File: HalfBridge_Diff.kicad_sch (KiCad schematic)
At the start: 3 parts, among them J5 Conn_01x04, U3 MAX3284E, U5 MAX3284E

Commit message: quad diff receiver
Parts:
- removed J5: Conn_01x04, Connector_Molex:Molex_PicoBlade_53261-0471_1x04-1MP_P1.25mm_Horizontal, symbol Connector_Generic:Conn_01x04
- added C2, C26, C3: 100n, Capacitor_SMD:C_0603_1608Metric_Pad1.08x0.95mm_HandSolder, symbol Device:C
- added J5: Conn_01x04_Shielded, My_Connector:Samtec_T1M-04-X-SH-L_1x04-1SH_P1.0mm_Terminal_Horizontal_Latch, symbol Connector_Generic_Shielded:Conn_01x04_Shielded
- added R18, R19: R, Resistor_SMD:R_0603_1608Metric_Pad0.98x0.95mm_HandSolder, symbol Device:R
- added U6: 74AUC2GU04, Package_TO_SOT_SMD:SOT-23-6_Handsoldering, symbol 74xGxx:74AUC2GU04
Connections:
- net gnd: now also C2.2, C26.1, C3.2, J5.SH (Shield), U6.2 (GND)
- net ina_d: now also U6.6; no longer U3.3 (RO)
- net ina_da: now also J5.4 (Pin_4), R18.1
- net ina_db: now also J5.3 (Pin_3), R18.2
- net inb_d: now also U6.4; no longer U5.3 (RO)
- net inb_da: now also J5.2 (Pin_2), R19.1
- net inb_db: now also J5.1 (Pin_1), R19.2
- net vcc: now also C2.1, C26.2, C3.1, U6.5 (VCC)
- new net ina_nd: U3.3 (RO), U6.1
- new net inb_nd: U5.3 (RO), U6.3
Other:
- moved on the sheet: U3

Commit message: not gate
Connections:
- net ina_d: now also U6.4; no longer U6.6
- net ina_nd: now also U6.3; no longer U6.1
- net inb_d: now also U6.6; no longer U6.4
- net inb_nd: now also U6.1; no longer U6.3
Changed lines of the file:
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@@
 		(lib_id "74xGxx:74AUC2GU04")
 		(at 161.29 109.22 0)
-		(unit 1)
+		(unit 2)
 		(exclude_from_sim no)
 		(in_bom yes)
@@
 				(path "/3c187ffa-7f66-4861-b077-b6965c821fc2/6db083ab-29ba-4c62-9810-6a6595b985fc"
 					(reference "U6")
-					(unit 1)
+					(unit 2)
 				)
 			)
@@
 		(lib_id "74xGxx:74AUC2GU04")
 		(at 161.29 142.24 0)
-		(unit 2)
+		(unit 1)
 		(exclude_from_sim no)
 		(in_bom yes)
@@
 				(path "/3c187ffa-7f66-4861-b077-b6965c821fc2/6db083ab-29ba-4c62-9810-6a6595b985fc"
 					(reference "U6")
-					(unit 2)
-				)
-			)
+					(unit 1)
+				)
+			)

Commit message: new optical diff xor
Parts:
- removed C26: 100n, Capacitor_SMD:C_0603_1608Metric_Pad1.08x0.95mm_HandSolder, symbol Device:C
- removed U6: 74AUC2GU04, Package_TO_SOT_SMD:SOT-23-6_Handsoldering, symbol 74xGxx:74AUC2GU04
- added J7: Conn_01x02, Connector_PinHeader_2.54mm:PinHeader_1x02_P2.54mm_Vertical, symbol Connector_Generic:Conn_01x02
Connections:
- net ina_nd is gone; now on net ina_d: U3.3 (RO)
- net inb_nd is gone; now on net inb_d: U5.3 (RO)
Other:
- moved on the sheet: C2, C3, R18, R19, U3, U5

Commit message: diff circuit
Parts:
- removed J5: Conn_01x04_Shielded, My_Connector:Samtec_T1M-04-X-SH-L_1x04-1SH_P1.0mm_Terminal_Horizontal_Latch, symbol Connector_Generic_Shielded:Conn_01x04_Shielded
- added C33: 100n, Capacitor_SMD:C_0603_1608Metric_Pad1.08x0.95mm_HandSolder, symbol Device:C
- added J10, J11, J12, J8, J9: Conn_01x02, Connector_PinHeader_2.54mm:PinHeader_1x02_P2.54mm_Vertical, symbol Connector_Generic:Conn_01x02
- added J14: Conn_01x02_Shielded, My_Connector:SAMTEC_T1M-02-F-SV-L-P, symbol Connector_Generic_Shielded:Conn_01x02_Shielded
- added R24: R, Resistor_SMD:R_0603_1608Metric_Pad0.98x0.95mm_HandSolder, symbol Device:R
- added R25, R26, R27: R, Resistor_SMD:R_0603_1608Metric, symbol Device:R
- added U9: MAX3284E, Package_TO_SOT_SMD:SOT-23-6_Handsoldering, symbol Interface_UART:MAX3284E
- J7: now not fitted
- renumbered C2 to C31, C3 to C32, R18 to R22, R19 to R23, U3 to U7, U5 to U8
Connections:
- net gnd: now also C33.2, J10.2 (Pin_2), J11.2 (Pin_2), J12.2 (Pin_2), J14.SH (Shield), U9.2 (GND)
- net ina_d: now also J10.1 (Pin_1), R25.2; no longer U7.3 (RO)
- net ina_da: now also J7.2 (Pin_2)
- net ina_db: now also J7.1 (Pin_1)
- net inb_d: now also J11.1 (Pin_1), R26.2; no longer U8.3 (RO)
- net inb_da: now also J14.2 (Pin_2), J8.2 (Pin_2)
- net inb_db: now also J14.1 (Pin_1), J8.1 (Pin_1)
- net vcc: now also U7.5 (VL), U8.5 (VL), C33.1, U9.1 (VCC), U9.5 (VL)
- new net ina_nd: R25.1, U7.3 (RO)
- new net inb_nd: R26.1, U8.3 (RO)
- new net inen_d: J12.1 (Pin_1), R27.2
- new net inen_da: J9.2 (Pin_2), R24.1, U9.6 (A)
- new net inen_db: J9.1 (Pin_1), R24.2, U9.4 (B)
- new net inen_nd: R27.1, U9.3 (RO)
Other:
- moved on the sheet: C31, C32, R22, R23, U7, U8

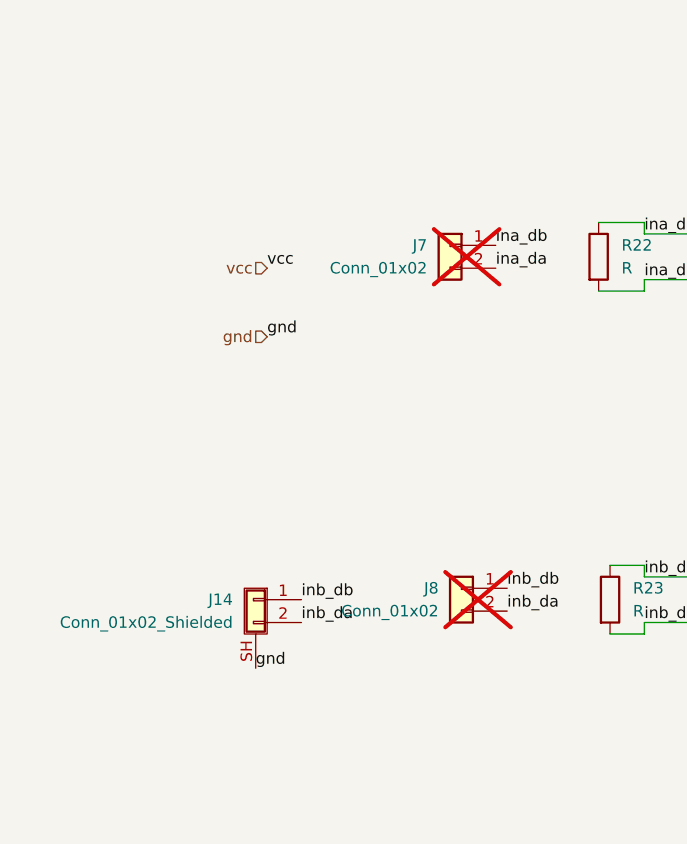
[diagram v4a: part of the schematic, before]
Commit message: horizontal connector
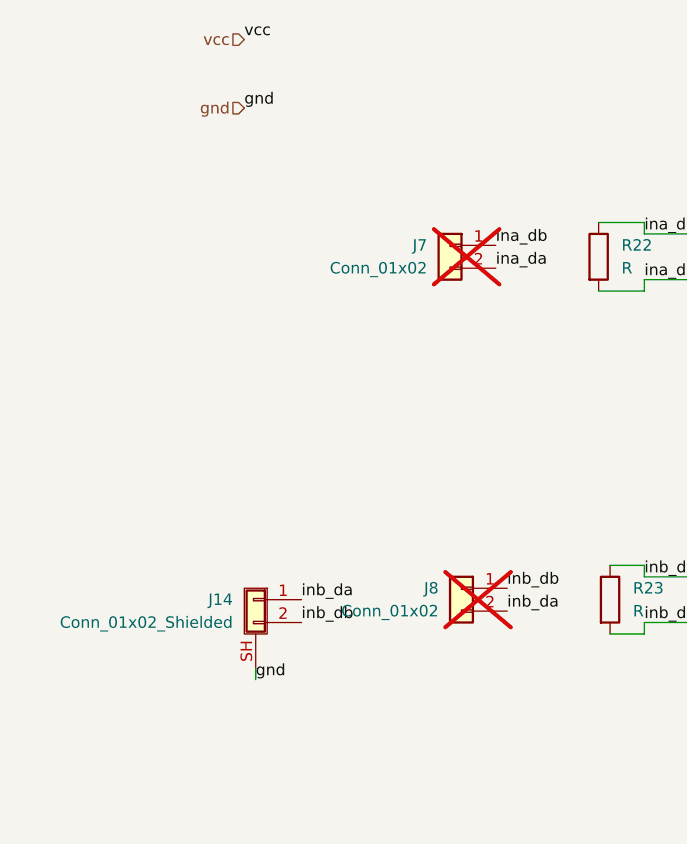
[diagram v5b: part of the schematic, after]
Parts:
- J14: footprint My_Connector:SAMTEC_T1M-02-F-SV-L-P -> My_Connector:SAMTEC_T1M-02-F-SH-L-K
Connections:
- net inb_da: now also J14.1 (Pin_1); no longer J14.2 (Pin_2)
- net inb_db: now also J14.2 (Pin_2); no longer J14.1 (Pin_1)
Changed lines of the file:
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@@
+	(wire
+		(pts
+			(xy 38.1 114.3) (xy 38.1 113.03)
+		)
+		(stroke
+			(width 0)
+			(type default)
+		)
+	)
 	(wire
 		(pts
@@
 	)
 	(label "gnd"
-		(at 38.1 113.03 0)
+		(at 38.1 114.3 0)
 		(fields_autoplaced yes)
 		(effects
@@
 		)
 	)
-	(label "inb_da"
+	(label "inb_db"
 		(at 43.18 107.95 0)
 		(fields_autoplaced yes)
@@
 	)
 	(label "vcc"
-		(at 39.37 68.58 0)
+		(at 36.83 43.18 0)
 		(fields_autoplaced yes)
 		(effects
@@
 	)
 	(label "gnd"
-		(at 39.37 76.2 0)
+		(at 36.83 50.8 0)
 		(fields_autoplaced yes)
 		(effects
@@
 		)
 	)
-	(label "inb_db"
+	(label "inb_da"
 		(at 43.18 105.41 0)
 		(fields_autoplaced yes)
@@
 	(hierarchical_label "vcc"
 		(shape input)
-		(at 39.37 68.58 180)
+		(at 36.83 43.18 180)
 		(fields_autoplaced yes)
 		(effects
@@
 	(hierarchical_label "gnd"
 		(shape input)
-		(at 39.37 76.2 180)
+		(at 36.83 50.8 180)
 		(fields_autoplaced yes)
 		(effects
@@
 			)
 		)
-		(property "Footprint" "My_Connector:SAMTEC_T1M-02-F-SV-L-P"
+		(property "Footprint" "My_Connector:SAMTEC_T1M-02-F-SH-L-K"
 			(at 38.1 105.41 0)
 			(effects
